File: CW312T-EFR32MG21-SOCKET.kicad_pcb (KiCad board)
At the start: 2 copper layers, 58.7 x 53.7 mm, 18 parts, among them J1 1x3 straight header pins, P1 PCIEx4 EDGE CONNECTOR, U1 EFR32MG21A020F1024IM32-BR

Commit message: first draft - ready for review
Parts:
- added PCB1: CE Symbol, Silkscrren_Symbols:CE-Logo_8.5x6mm_SilkScreen, F.Cu at (116.6, 106.9)
- added PCB2: Pb_Free Symbol, Silkscrren_Symbols:Pb_Free_8.0x8.0mm_SilkScreen, F.Cu at (115.4, 99.0)
- added PCB3: UKCA symbol, Silkscrren_Symbols:UKCA-Logo_8x8mm_SilkScreen, F.Cu at (115.6, 89.6)
- added PCB4: WEEE SYMBOL, Silkscrren_Symbols:WEEE-Logo_5.6x8mm_SilkScreen, F.Cu at (115.2, 114.4)
- moved R2 3.68 mm to (119.5, 101.5)
- moved C7 3.35 mm to (142.2, 84.2)
- moved C3 3.35 mm to (146.7, 83.5)
- moved C5 3.35 mm to (148.3, 83.5)
- moved L1 3.35 mm to (144.8, 83.5)
- moved SJ4 3.35 mm to (150.7, 83.7)
- moved C4 1.72 mm to (151.6, 80.8), turned to 180 degrees
- moved SJ3 1.50 mm to (117.6, 109.8)
- moved C6 1.50 mm to (119.9, 109.9)
- moved C1 1.00 mm to (154.0, 92.5)
- moved C2 1.00 mm to (154.0, 90.8)
- moved J1 1.00 mm to (155.4, 105.1)
- moved R1 1.00 mm to (154.8, 95.4)
- moved SJ1 1.00 mm to (154.1, 88.0)
- moved SJ2 1.00 mm to (155.5, 110.2)
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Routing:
- net +3V3: track 3.13 -> 115.0 mm, vias 0 -> 5
- net GND: track 37.7 -> 62.5 mm, vias 0 -> 12
- net /TDO: track 41.1 -> 35.3 mm
- net /TDI: track 46.6 -> 41.3 mm
- net /CLKIN: track 18.4 -> 14.0 mm
- net /FILT: track 21.2 -> 17.3 mm
- net Net-(P1-FILTIN): track 11.2 -> 7.77 mm
- net /GPIO1: track 36.4 -> 33.2 mm
- net /GPIO3: track 38.2 -> 35.2 mm
- net /SWCLK: track 49.4 -> 48.1 mm
- net Net-(U1-DVDD): track 19.9 -> 18.6 mm
- net /GPIO4: track 32.4 -> 31.5 mm
- net /SWDIO: track 43.1 -> 42.1 mm
- net Net-(U1-AVDD): track 14.8 -> 15.7 mm
- net /RST: track 63.1 -> 62.3 mm
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- added copper zone on B.Cu, net GND
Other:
- board text added: "DVCC"
- board text added: "EFR32MG21-SOCKET Target For CW312T Board"
- board text added: "NewAE Technology Inc. CW312T-EFR32MG21-SOCKET RoHS / Pb Free"
- board text added: "PAVCC"
- board text added: "RFVCC"
- board text added: "original board has newae logo should this be included? other targets havent included this"

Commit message: updated schematic, pcb and production files - Ready for review
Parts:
- moved C1 1.65 mm to (154.0, 94.2)
- moved C2 1.65 mm to (154.0, 92.5)
- moved C6 1.65 mm to (120.0, 111.6)
- moved C7 1.65 mm to (142.2, 85.9)
- moved C8 1.65 mm to (153.3, 112.0)
- moved R1 1.65 mm to (154.8, 97.1)
- moved R2 1.65 mm to (119.5, 103.1)
- moved SJ1 1.65 mm to (154.2, 89.7)
- moved SJ2 1.65 mm to (155.5, 111.9)
- moved SJ3 1.65 mm to (117.7, 111.5)
- moved U1 1.65 mm to (131.1, 100.8)
- moved J1 1.65 mm to (155.4, 106.8)
- moved C3 1.65 mm to (146.7, 85.2)
- moved C5 1.65 mm to (148.4, 85.2)
- moved L1 1.65 mm to (144.9, 85.2)
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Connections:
- P1 pad A26: unconnected-(P1-JTAG_VREF-PadA26) -> +3V3
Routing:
- net +3V3: track 115.0 -> 143.0 mm, vias 5 -> 8
- net /TDO: track 35.3 -> 37.8 mm
- net /SWDIO: track 42.1 -> 44.0 mm
- net /SWCLK: track 48.1 -> 50.0 mm
- net Net-(P1-CLKOUT): track 33.1 -> 34.9 mm
- net /GPIO4: track 31.5 -> 33.2 mm
- net /FILT: track 17.3 -> 19.1 mm
- net /GPIO3: track 35.2 -> 36.9 mm
- net /GPIO2: track 34.3 -> 36.0 mm
- net /GPIO1: track 33.2 -> 34.9 mm
- net /SHUNTH: track 30.3 -> 32.0 mm
- net /SHUNTL: track 37.8 -> 39.4 mm
- net /TDI: track 41.3 -> 42.9 mm
- net /RST: track 62.3 -> 63.6 mm
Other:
- board text added: "RST"
- board text added: "VREF"
- board text added: "original board has newae logo on front silkscreen should this be included? other targets havent included this"
- board text removed: "What to do with the 34 and 35 pads on this footprint the gerbers for the old design has these pads as well but they arent in the schematic"
- board text removed: "original board has newae logo should this be included? other targets havent included this"

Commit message: updated silkscreen and production files
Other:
- board text added: "+3V3"
- board text removed: "VREF"
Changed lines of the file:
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@@
 		)
 	)
-	(gr_text "VREF"
-		(at 148.2 81.35 90)
+	(gr_text "+3V3"
+		(at 148.25 81.8 90)
 		(layer "F.SilkS")
 		(effects

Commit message: updated 3 pin header to fix footprint
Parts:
- J1: footprint Connector_PinHeader_1.00mm:PinHeader_1x03_P1.00mm_Vertical -> Connector_PinHeader_2.54mm:PinHeader_1x03_P2.54mm_Vertical
- moved J1 3.86 mm to (154.6, 103.0)
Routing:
- net Net-(U1-RF2G4_IO2): track 20.0 -> 19.3 mm
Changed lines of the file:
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@@
 		)
 	)
-	(footprint "Connector_PinHeader_1.00mm:PinHeader_1x03_P1.00mm_Vertical"
+	(footprint "Connector_PinHeader_2.54mm:PinHeader_1x03_P2.54mm_Vertical"
 		(layer "F.Cu")
-		(at 155.3961 106.753899)
-		(descr "Through hole straight pin header, 1x03, 1.00mm pitch, single row")
-		(tags "Through hole pin header THT 1x03 1.00mm single row")
+		(at 154.625 102.97)
+		(descr "Through hole straight pin header, 1x03, 2.54mm pitch, single row")
+		(tags "Through hole pin header THT 1x03 2.54mm single row")
 		(property "Reference" "J1"
-			(at 0 -1.653899 0)
+			(at 0 -2.33 0)
 			(layer "F.SilkS")
 			(effects
@@
 		)
 		(property "Value" "1x3 straight header pins"
-			(at 0 3.56 0)
+			(at 0 7.41 0)
 			(layer "F.Fab")
 			(effects
@@
 			)
 		)
-		(property "Footprint" "Connector_PinHeader_1.00mm:PinHeader_1x03_P1.00mm_Vertical"
+		(property "Footprint" "Connector_PinHeader_2.54mm:PinHeader_1x03_P2.54mm_Vertical"
 			(at 0 0 0)
 			(unlocked yes)
@@
 		(attr through_hole)
 		(fp_line
-			(start -0.695 -0.685)
-			(end 0 -0.685)
+			(start -1.33 -1.33)
+			(end 0 -1.33)
 			(stroke
 				(width 0.12)
@@
 		)
 		(fp_line
-			(start -0.695 0)
-			(end -0.695 -0.685)
+			(start -1.33 0)
+			(end -1.33 -1.33)
 			(stroke
 				(width 0.12)
@@
 		)
 		(fp_line
-			(start -0.695 0.685)
-			(end -0.695 2.56)
+			(start -1.33 1.27)
+			(end -1.33 6.41)
 			(stroke
 				(width 0.12)
@@
 		)
 		(fp_line
-			(start -0.695 0.685)
-			(end -0.608276 0.685)
+			(start -1.33 1.27)
+			(end 1.33 1.27)
 			(stroke
 				(width 0.12)
@@
 		)
 		(fp_line
-			(start -0.695 2.56)
-			(end -0.394493 2.56)
+			(start -1.33 6.41)
+			(end 1.33 6.41)
 			(stroke
 				(width 0.12)
@@
 		)
 		(fp_line
-			(start 0.394493 2.56)
-			(end 0.695 2.56)
+			(start 1.33 1.27)
+			(end 1.33 6.41)
 			(stroke
 				(width 0.12)
@@
 		)
 		(fp_line
-			(start 0.608276 0.685)
-			(end 0.695 0.685)
-			(stroke
-				(width 0.12)
-				(type solid)
-			)
-			(layer "F.SilkS")
-		)
-		(fp_line
-			(start 0.695 0.685)
-			(end 0.695 2.56)
-			(stroke
-				(width 0.12)
-				(type solid)
-			)
-			(layer "F.SilkS")
-		)
-		(fp_line
-			(start -1.15 -1)
-			(end -1.15 3)
+			(start -1.8 -1.8)
+			(end -1.8 6.85)
 			(stroke
 				(width 0.05)
@@
 		)
 		(fp_line
-			(start -1.15 3)
-			(end 1.15 3)
+			(start -1.8 6.85)
+			(end 1.8 6.85)
 			(stroke
 				(width 0.05)
@@
 		)
 		(fp_line
-			(start 1.15 -1)
-			(end -1.15 -1)
+			(start 1.8 -1.8)
+			(end -1.8 -1.8)
 			(stroke
 				(width 0.05)
@@
 		)
 		(fp_line
-			(start 1.15 3)
-			(end 1.15 -1)
+			(start 1.8 6.85)
+			(end 1.8 -1.8)
 			(stroke
 				(width 0.05)
@@
 		)
 		(fp_line
-			(start -0.635 -0.1825)
-			(end -0.3175 -0.5)
+			(start -1.27 -0.635)
+			(end -0.635 -1.27)
 			(stroke
 				(width 0.1)
@@
 		)
 		(fp_line
-			(start -0.635 2.5)
-			(end -0.635 -0.1825)
+			(start -1.27 6.35)
+			(end -1.27 -0.635)
 			(stroke
 				(width 0.1)
@@
 		)
 		(fp_line
-			(start -0.3175 -0.5)
-			(end 0.635 -0.5)
+			(start -0.635 -1.27)
+			(end 1.27 -1.27)
 			(stroke
 				(width 0.1)
@@
 		)
 		(fp_line
-			(start 0.635 -0.5)
-			(end 0.635 2.5)
+			(start 1.27 -1.27)
+			(end 1.27 6.35)
 			(stroke
 				(width 0.1)
@@
 		)
 		(fp_line
-			(start 0.635 2.5)
-			(end -0.635 2.5)
+			(start 1.27 6.35)
+			(end -1.27 6.35)
 			(stroke
 				(width 0.1)
@@
 		)
 		(fp_text user "${REFERENCE}"
-			(at 0 1 90)
+			(at 0 2.54 90)
 			(layer "F.Fab")
 			(effects
 				(font
-					(size 0.76 0.76)
-					(thickness 0.114)
+					(size 1 1)
+					(thickness 0.15)
 				)
 			)
@@
 		(pad "1" thru_hole rect
 			(at 0 0)
-			(size 0.85 0.85)
-			(drill 0.5)
+			(size 1.7 1.7)
+			(drill 1)
 			(layers "*.Cu" "*.Mask")
 			(remove_unused_layers no)
@@
 		)
 		(pad "2" thru_hole oval
-			(at 0 1)
-			(size 0.85 0.85)
-			(drill 0.5)
+			(at 0 2.54)
+			(size 1.7 1.7)
+			(drill 1)
 			(layers "*.Cu" "*.Mask")
 			(remove_unused_layers no)
@@
 		)
 		(pad "3" thru_hole oval
-			(at 0 2)
-			(size 0.85 0.85)
-			(drill 0.5)
+			(at 0 5.08)
+			(size 1.7 1.7)
+			(drill 1)
 			(layers "*.Cu" "*.Mask")
 			(remove_unused_layers no)
@@
 			(pintype "unspecified")
 		)
-		(model "${KICAD8_3DMODEL_DIR}/Connector_PinHeader_1.00mm.3dshapes/PinHeader_1x03_P1.00mm_Vertical.wrl"
+		(model "${KICAD8_3DMODEL_DIR}/Connector_PinHeader_2.54mm.3dshapes/PinHeader_1x03_P2.54mm_Vertical.wrl"
 			(offset
 				(xyz 0 0 0)
@@
 	)
 	(segment
-		(start 140.075 106.75)
-		(end 141.078899 107.753899)
+		(start 136.40038 108.199999)
+		(end 137.850379 106.75)
 		(width 0.3)
 		(layer "F.Cu")
@@
 	)
 	(segment
-		(start 136.40038 108.199999)
-		(end 137.850379 106.75)
+		(start 150.65 106.75)
+		(end 151.89 105.51)
 		(width 0.3)
 		(layer "F.Cu")
@@
 	)
 	(segment
-		(start 141.078899 107.753899)
-		(end 155.3961 107.753899)
+		(start 151.89 105.51)
+		(end 154.625 105.51)
 		(width 0.3)
 		(layer "F.Cu")
@@
 	(segment
 		(start 137.850379 106.75)
-		(end 140.075 106.75)
+		(end 150.65 106.75)
 		(width 0.3)
 		(layer "F.Cu")
@@
 	)
 	(segment
-		(start 139.325 110.5461)
-		(end 138.051433 110.5461)
-		(width 0.2)
+		(start 154.85 108.05)
+		(end 154.625 108.05)
+		(width 0.3)
 		(layer "F.Cu")
 		(net 8)
@@
 	(segment
 		(start 139.325 110.5461)
-		(end 139.3289 110.5461)
-		(width 0.3)
+		(end 138.051433 110.5461)
+		(width 0.2)
 		(layer "F.Cu")
 		(net 8)
 	)
 	(segment
-		(start 139.3289 110.5461)
-		(end 141.1211 108.7539)
+		(start 149.6539 110.5461)
+		(end 139.325 110.5461)
 		(width 0.3)
 		(layer "F.Cu")
@@
 	)
 	(segment
-		(start 155.35 108.8)
-		(end 155.3961 108.7539)
-		(width 0.2)
+		(start 154.625 108.05)
+		(end 152.15 108.05)
+		(width 0.3)
 		(layer "F.Cu")
 		(net 8)
 	)
 	(segment
-		(start 141.1211 108.7539)
-		(end 155.3961 108.7539)
+		(start 152.15 108.05)
+		(end 149.6539 110.5461)
 		(width 0.3)
 		(layer "F.Cu")

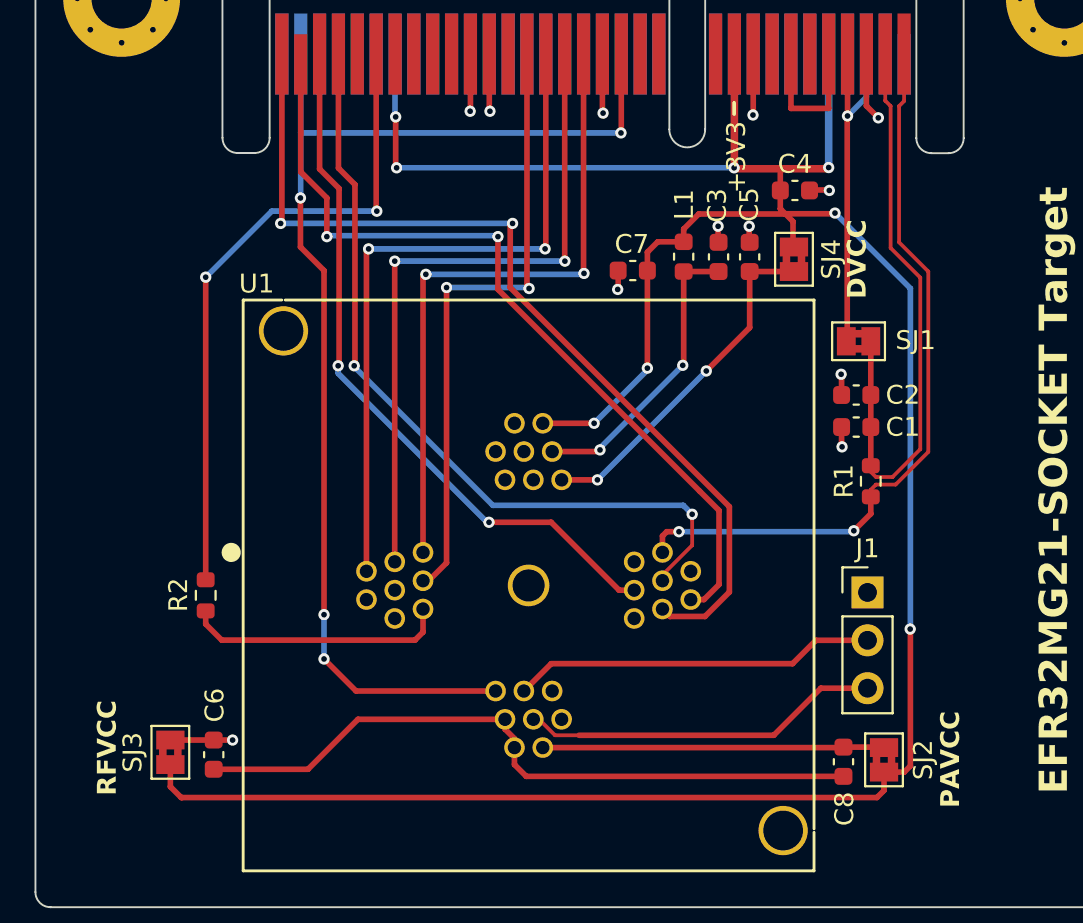
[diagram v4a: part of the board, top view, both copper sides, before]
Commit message: updated schematic and pcb after library re-organization
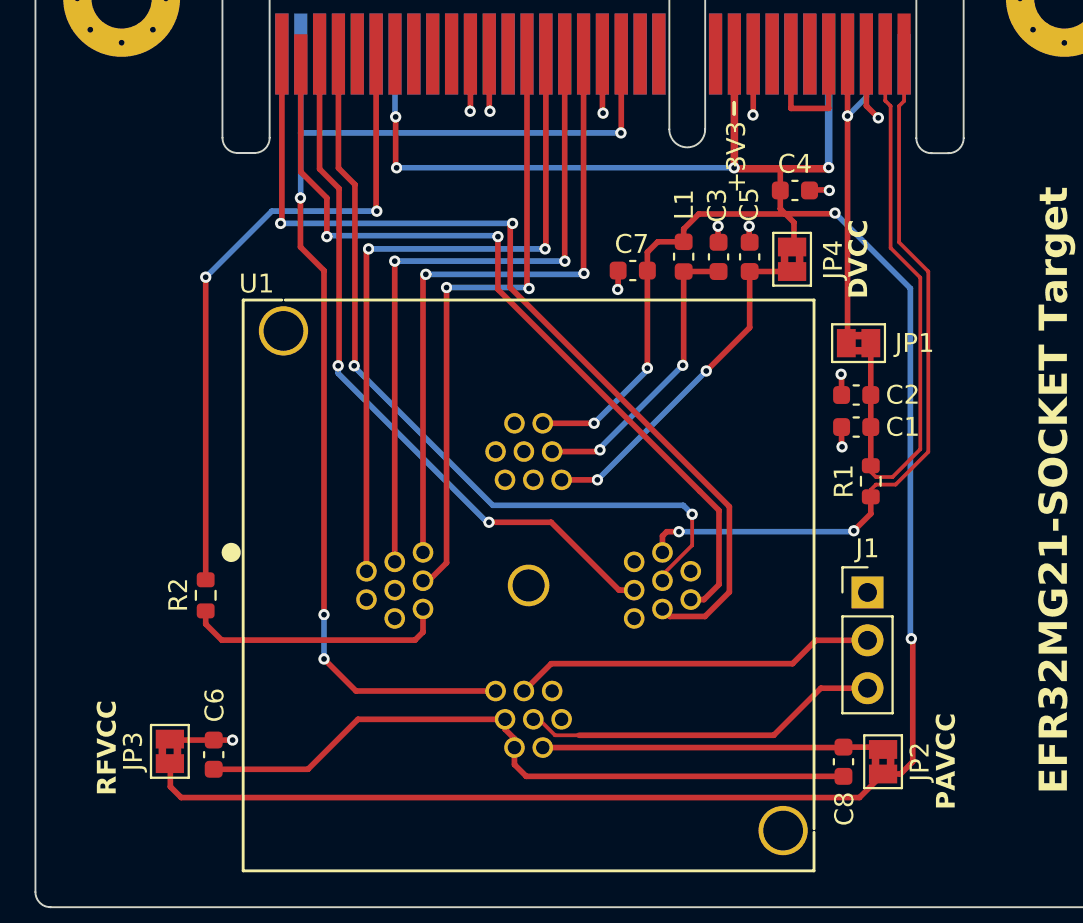
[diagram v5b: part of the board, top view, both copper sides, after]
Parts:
- removed SJ1, SJ2, SJ3, SJ4: ~, Jumper:SolderJumper-2_P1.3mm_Bridged2Bar_Pad1.0x1.5mm
- added JP1: ~, Jumper:SolderJumper-2_P1.3mm_Bridged2Bar_Pad1.0x1.5mm, F.Cu at (154.2, 89.8)
- added JP2: ~, Jumper:SolderJumper-2_P1.3mm_Bridged2Bar_Pad1.0x1.5mm, F.Cu at (155.4, 112.0)
- added JP3: ~, Jumper:SolderJumper-2_P1.3mm_Bridged2Bar_Pad1.0x1.5mm, F.Cu at (117.6, 111.4)
- added JP4: ~, Jumper:SolderJumper-2_P1.3mm_Bridged2Bar_Pad1.0x1.5mm, F.Cu at (150.6, 85.3)
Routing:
- net +3V3: track 143.0 -> 142.5 mm
